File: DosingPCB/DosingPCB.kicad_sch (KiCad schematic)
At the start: 4 parts, among them U1 SHTC3

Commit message: Basically finished schematic
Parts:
- added C1, C4: 22uF, Capacitor_SMD:C_1206_3216Metric, symbol Device:C
- added C2, C5, C6: .1uF, Capacitor_SMD:C_0603_1608Metric, symbol Device:C
- added C3: 10uF, Capacitor_SMD:C_0805_2012Metric, symbol Device:C
- added D1: Green, LED_SMD:LED_0603_1608Metric, symbol Device:LED
- added D2: 1N4148WT, Diode_SMD:D_SOD-523, symbol Diode:1N4148WT
- added D3: 1N5817, Diode_THT:D_DO-41_SOD81_P10.16mm_Horizontal, symbol Diode:1N5817
- added J1: Conn_01x06_Pin, Connector_PinHeader_1.00mm:PinHeader_1x06_P1.00mm_Vertical, symbol Connector:Conn_01x06_Pin
- added J2: STLink, Connector_PinHeader_1.00mm:PinHeader_1x02_P1.00mm_Vertical, symbol Connector:Conn_01x02_Pin
- added J3: Servo Conn, Connector_PinHeader_1.00mm:PinHeader_1x03_P1.00mm_Horizontal, symbol Connector:Conn_01x03_Pin
- added J4: SPI header, Connector_PinHeader_1.00mm:PinHeader_1x08_P1.00mm_Vertical, symbol Connector:Conn_01x08_Pin
- added J5: USB_C_Receptacle_USB2.0_16P, Connector_USB:USB_C_Receptacle_GCT_USB4105-xx-A_16P_TopMnt_Horizontal, symbol Connector:USB_C_Receptacle_USB2.0_16P
- added J8: Solar Cell JST, Connector_JST:JST_PH_S2B-PH-K_1x02_P2.00mm_Horizontal, symbol Connector_Generic:Conn_01x02
- added J9: 5V fan JST, Connector_Molex:Molex_KK-254_AE-6410-03A_1x03_P2.54mm_Vertical, symbol Connector_Generic:Conn_01x03
- added Q1: MMBT2222A, Package_TO_SOT_SMD:SOT-23, symbol Transistor_BJT:MMBT2222A
- added R1: 10k, Resistor_SMD:R_0805_2012Metric, symbol Device:R
- added R2: 470, Resistor_SMD:R_0805_2012Metric, symbol Device:R
- added R3: 1K, Resistor_SMD:R_0805_2012Metric, symbol Device:R
- added R6, R7: 5.1k, Resistor_SMD:R_0805_2012Metric, symbol Device:R
- added SW1: SW_Push, Button_Switch_SMD:SW_SPST_TL3342, symbol Switch:SW_Push
- added SW2: SW_SPDT, Button_Switch_SMD:SW_SPDT_PCM12, symbol Switch:SW_SPDT
- added U1: AMS1117-3.3, Package_TO_SOT_SMD:SOT-223-3_TabPin2, symbol Regulator_Linear:AMS1117-3.3
- added U2: STM32L432KBUx, Package_DFN_QFN:QFN-32-1EP_5x5mm_P0.5mm_EP3.45x3.45mm, symbol MCU_ST_STM32L4:STM32L432KBUx
- added U4: D3V3XA4B10LP, Package_DFN_QFN:Diodes_UDFN-10_1x2.5mm_P0.5mm, symbol Power_Protection:D3V3XA4B10LP
- R4: footprint (none) -> Resistor_SMD:R_0805_2012Metric
- R5: renamed from R3; footprint (none) -> Resistor_SMD:R_0805_2012Metric
- renumbered U1 to U3
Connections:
- net +3.3V: now also C3.1, C4.1, C5.1, C6.1, D1.2 (A), J1.6 (Pin_6), J3.2 (Pin_2), J4.7 (Pin_7), SW2.3 (C), U1.2 (VO), U2.1 (VDD), U2.17 (VDD), U2.5 (VDDA)
- net CS: now also U2.25 (PA15)
- net GND: now also C1.2, C2.1, C3.2, C4.2, C5.2, C6.2, J1.1 (Pin_1), J3.3 (Pin_3), J4.1 (Pin_1), J5.A1 (GND), J5.A12 (GND), J5.B1 (GND), J5.B12 (GND), J5.SH (SHIELD), J8.2 (Pin_2), Q1.2 (E), R2.2, R6.2, R7.2, SW1.1, SW2.1 (A), U1.1 (GND), U2.16 (VSS), U2.32 (VSS), U2.33 (VSS), U4.3 (VSS), U4.8 (VSS)
- net RTC_SCL: now also U2.19 (PA9)
- net RTC_SDA: now also U2.20 (PA10)
- net SD_CLK: now also U2.26 (PB3)
- net SD_DataIn: now also U2.28 (PB5)
- net SD_DataOut: now also U2.27 (PB4)
- net Solar+Charging/VIN/Solar+: now also J8.1 (Pin_1)
- net Temp_SCL: now also U2.29 (PB6)
- net Temp_SDA: now also U2.30 (PB7)
- new net: D2.2 (A), J9.3 (Pin_3), Q1.3 (C)
- new net: Q1.1 (B), R3.2
- new net: J1.2 (Pin_2), U2.2 (PC14)
- new net: J1.3 (Pin_3), U2.3 (PC15)
- new net: J1.4 (Pin_4), U2.14 (PB0)
- new net: J1.5 (Pin_5), U2.15 (PB1)
- new net: R1.2, SW2.2 (B)
- new net: C2.2, SW1.2, U2.4 (NRST)
- new net: J4.2 (Pin_2), U2.13 (PA7)
- new net: J4.3 (Pin_3), U2.12 (PA6)
- new net: J4.4 (Pin_4), U2.11 (PA5)
- new net: J4.5 (Pin_5), U2.10 (PA4)
- new net: J4.6 (Pin_6), U2.7 (PA1)
- new net: J3.1 (Pin_1), U2.18 (PA8)
- new net: J9.1 (Pin_1), U2.9 (PA3)
- new net: R1.1, U2.31 (PH3)
- new net: R3.1, U2.8 (PA2)
- new net: D3.2 (A), J5.A4 (VBUS), J5.A9 (VBUS), J5.B4 (VBUS), J5.B9 (VBUS)
- new net: J5.A5 (CC1), R6.1
- new net: J5.A6 (D+), J5.B6 (D+), U4.1
- new net: J5.A7 (D-), J5.B7 (D-), U4.2, U4.9 (NC)
- new net: J5.B5 (CC2), R7.1
- new net: D1.1 (K), R2.1
- new net +5V: C1.1, D2.1 (K), D3.1 (K), J4.8 (Pin_8), J9.2 (Pin_2), U1.3 (VI)
- new net CD: U2.6 (PA0)
- new net Data+: U2.22 (PA12), U4.5
- new net Data-: U2.21 (PA11), U4.4
- new net SWCLK: J2.1 (Pin_1), U2.24 (PA14)
- new net SWDIO: J2.2 (Pin_2), U2.23 (PA13)
- no-connect marks 0 -> 5
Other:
- sheet SD-Card ports: added CD; removed none
- note added: "Check JST size with Fan and check pin orientation"
- note added: "Check JST size with Solar cell and check pin orientation"
- moved on the sheet: R4, R5, SC1, U3

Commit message: Starting Board setup
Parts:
- D3: footprint Diode_THT:D_DO-41_SOD81_P10.16mm_Horizontal -> Diode_SMD:D_SOD-123
- SW1: footprint Button_Switch_SMD:SW_SPST_TL3342 -> Button_Switch_SMD:SW_Push_SPST_NO_CK_KSC
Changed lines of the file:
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@@
 	)
 	(junction
-		(at 31.75 29.21)
-		(diameter 0)
-		(color 0 0 0 0)
-	)
-	(junction
 		(at 52.07 91.44)
 		(diameter 0)
@@
 	)
 	(junction
-		(at 52.07 26.67)
+		(at 77.47 96.52)
 		(diameter 0)
 		(color 0 0 0 0)
 	)
 	(junction
-		(at 77.47 96.52)
+		(at 254 71.12)
 		(diameter 0)
 		(color 0 0 0 0)
 	)
 	(junction
-		(at 254 71.12)
+		(at 31.75 29.21)
+		(diameter 0)
+		(color 0 0 0 0)
+	)
+	(junction
+		(at 52.07 26.67)
 		(diameter 0)
 		(color 0 0 0 0)
@@
 	(wire
 		(pts
+			(xy 31.75 26.67) (xy 31.75 29.21)
+		)
+		(stroke
+			(width 0)
+			(type default)
+		)
+	)
+	(wire
+		(pts
 			(xy 52.07 99.06) (xy 62.23 99.06)
 		)
@@
 	(wire
 		(pts
-			(xy 52.07 24.13) (xy 52.07 26.67)
+			(xy 52.07 21.59) (xy 52.07 26.67)
 		)
 		(stroke
@@
 		)
 	)
+	(label "5V"
+		(at 31.75 27.94 0)
+		(effects
+			(font
+				(size 1.27 1.27)
+			)
+			(justify left bottom)
+		)
+	)
 	(global_label "Temp_SDA"
 		(shape input)
@@
 		(dnp no)
 		(property "Reference" "SW1"
-			(at 30.48 121.9199 90)
+			(at 14.732 108.458 90)
 			(show_name no)
 			(do_not_autoplace no)
@@
 		)
 		(property "Value" "SW_Push"
-			(at 30.48 124.4599 90)
+			(at 14.732 110.998 90)
 			(show_name no)
 			(do_not_autoplace no)
@@
 			)
 		)
-		(property "Footprint" "Button_Switch_SMD:SW_SPST_TL3342"
+		(property "Footprint" "Button_Switch_SMD:SW_Push_SPST_NO_CK_KSC"
 			(at 21.59 109.22 0)
 			(hide yes)
@@
 	(symbol
 		(lib_id "power:+3.3V")
-		(at 52.07 24.13 0)
+		(at 52.07 21.59 0)
 		(unit 1)
 		(body_style 1)
@@
 		(fields_autoplaced yes)
 		(property "Reference" "#PWR08"
-			(at 52.07 27.94 0)
+			(at 52.07 25.4 0)
 			(hide yes)
 			(show_name no)
@@
 		)
 		(property "Value" "+3.3V"
-			(at 52.07 19.05 0)
+			(at 52.07 16.51 0)
 			(show_name no)
 			(do_not_autoplace no)
@@
 		)
 		(property "Footprint" ""
-			(at 52.07 24.13 0)
+			(at 52.07 21.59 0)
 			(hide yes)
 			(show_name no)
@@
 		)
 		(property "Datasheet" ""
-			(at 52.07 24.13 0)
+			(at 52.07 21.59 0)
 			(hide yes)
 			(show_name no)
@@
 		)
 		(property "Description" "Power symbol creates a global label with name \"+3.3V\""
-			(at 52.07 24.13 0)
+			(at 52.07 21.59 0)
 			(hide yes)
 			(show_name no)
@@
 			)
 		)
-		(property "Footprint" "Diode_THT:D_DO-41_SOD81_P10.16mm_Horizontal"
+		(property "Footprint" "Diode_SMD:D_SOD-123"
 			(at 200.66 89.535 0)
 			(hide yes)
@@
 	(symbol
 		(lib_id "power:+5V")
-		(at 31.75 29.21 0)
+		(at 31.75 26.67 0)
 		(unit 1)
 		(body_style 1)
@@
 		(dnp no)
 		(property "Reference" "#PWR02"
-			(at 31.75 33.02 0)
+			(at 31.75 30.48 0)
 			(hide yes)
 			(show_name no)
@@
 		)
 		(property "Value" "+5V"
-			(at 29.464 24.638 0)
+			(at 29.464 22.098 0)
 			(show_name no)
 			(do_not_autoplace no)
@@
 		)
 		(property "Footprint" ""
-			(at 31.75 29.21 0)
+			(at 31.75 26.67 0)
 			(hide yes)
 			(show_name no)
@@
 		)
 		(property "Datasheet" ""
-			(at 31.75 29.21 0)
+			(at 31.75 26.67 0)
 			(hide yes)
 			(show_name no)
@@
 		)
 		(property "Description" "Power symbol creates a global label with name \"+5V\""
-			(at 31.75 29.21 0)
+			(at 31.75 26.67 0)
 			(hide yes)
 			(show_name no)

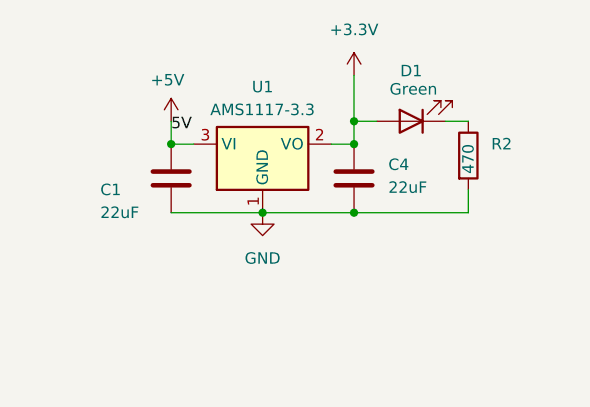
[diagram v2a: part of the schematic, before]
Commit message: Quick RTC fix
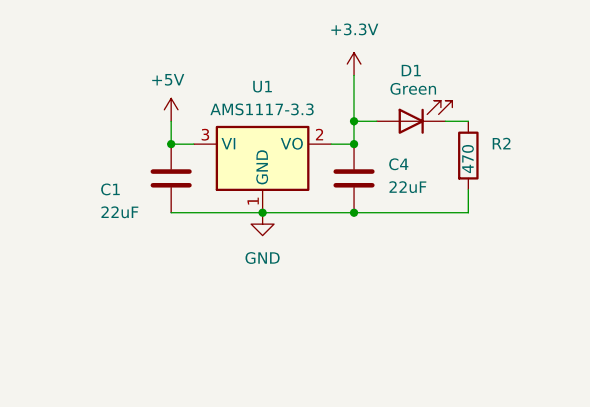
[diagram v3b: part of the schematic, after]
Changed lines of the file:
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@@
-		)
-	)
-	(label "5V"
-		(at 31.75 27.94 0)
-		(effects
-			(font
-				(size 1.27 1.27)
-			)
-			(justify left bottom)
 		)
 	)

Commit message: 98% completed PCB
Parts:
- removed R1: 10k, Resistor_SMD:R_0805_2012Metric, symbol Device:R
- added C16: 10uF, Capacitor_SMD:C_0805_2012Metric, symbol Device:C
- added C17, C25, C26: .1uF, Capacitor_SMD:C_0603_1608Metric, symbol Device:C
- added H4, H5, H6, H7, H8: MountingHole, MountingHole:MountingHole_2.2mm_M2, symbol Mechanical:MountingHole
- added J10, J11: Conn_01x04, Connector_JST:JST_SH_SM04B-SRSS-TB_1x04-1MP_P1.00mm_Horizontal, symbol Connector_Generic:Conn_01x04
- added R26: 10k, Resistor_SMD:R_0805_2012Metric, symbol Device:R
- J1: footprint Connector_PinHeader_1.00mm:PinHeader_1x06_P1.00mm_Vertical -> Connector_PinHeader_2.54mm:PinHeader_1x06_P2.54mm_Vertical
- J2: footprint Connector_PinHeader_1.00mm:PinHeader_1x02_P1.00mm_Vertical -> Connector_PinHeader_2.54mm:PinHeader_1x02_P2.54mm_Vertical
- J3: footprint Connector_PinHeader_1.00mm:PinHeader_1x03_P1.00mm_Horizontal -> Connector_PinHeader_2.54mm:PinHeader_1x03_P2.54mm_Horizontal
- J4: footprint Connector_PinHeader_1.00mm:PinHeader_1x08_P1.00mm_Vertical -> Connector_PinHeader_2.54mm:PinHeader_1x08_P2.54mm_Vertical
- SW1: footprint Button_Switch_SMD:SW_Push_SPST_NO_CK_KSC -> Button_Switch_SMD:SW_Push_SPST_NO_Alps_SKRK
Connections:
- net +3.3V: now also C16.2, C17.1, C25.1, J10.2 (Pin_2), J11.3 (Pin_3); no longer J3.2 (Pin_2)
- net +5V: now also J3.2 (Pin_2), C26.1
- net CD: now also U2.14 (PB0); no longer U2.6 (PA0)
- net GND: now also C16.1, C17.2, C25.2, C26.2, J10.1 (Pin_1), J11.4 (Pin_4), R26.1
- net Temp_SCL: now also R4.1, U3.3 (SDA), J10.4 (Pin_4), J11.1 (Pin_1); no longer R5.1, U3.2 (SCL)
- net Temp_SDA: now also R5.1, U3.2 (SCL), J10.3 (Pin_3), J11.2 (Pin_2); no longer R4.1, U3.3 (SDA)
- net header conn: now reaches J1.4 (Pin_4)
- net header conn: now also U2.6 (PA0); no longer U2.14 (PB0)
- net at SW2.2 (B): now also U2.31 (PH3), R26.2
- net Solar+Charging/VIN/Solar+ renamed Solar_power
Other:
- moved on the sheet: C1, C4, D1, D3, J8, R2, U1

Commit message: Finished PCB - mousebites
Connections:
- net at J1.5 (Pin_5): no longer U2.15 (PB1)
- net header conn: no longer names the net of J1.4 (Pin_4)
- net header conn: no longer U2.6 (PA0)
- no-connect marks 5 -> 9
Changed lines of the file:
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@@
+	)
+	(no_connect
+		(at 92.71 104.14)
 	)
 	(no_connect
@@
 	)
 	(no_connect
+		(at 66.04 168.91)
+	)
+	(no_connect
 		(at 208.28 133.35)
+	)
+	(no_connect
+		(at 67.31 124.46)
 	)
 	(no_connect
@@
 		(at 198.12 125.73)
 	)
+	(no_connect
+		(at 63.5 168.91)
+	)
 	(wire
 		(pts
@@
 	(wire
 		(pts
-			(xy 66.04 124.46) (xy 66.04 168.91)
-		)
-		(stroke
-			(width 0)
-			(type default)
-		)
-	)
-	(wire
-		(pts
 			(xy 219.71 27.94) (xy 223.52 27.94)
 		)
@@
 		(pts
 			(xy 31.75 137.16) (xy 31.75 142.24)
-		)
-		(stroke
-			(width 0)
-			(type default)
-		)
-	)
-	(wire
-		(pts
-			(xy 67.31 124.46) (xy 66.04 124.46)
 		)
 		(stroke
@@
 		)
 	)
-	(global_label "header conn"
-		(shape input)
-		(at 63.5 168.91 90)
-		(fields_autoplaced yes)
-		(effects
-			(font
-				(size 1.27 1.27)
-			)
-			(justify left)
-		)
-		(property "Intersheetrefs" "${INTERSHEET_REFS}"
-			(at 63.5 154.0112 90)
-			(hide yes)
-			(show_name no)
-			(do_not_autoplace no)
-			(effects
-				(font
-					(size 1.27 1.27)
-				)
-				(justify left)
-			)
-		)
-	)
 	(global_label "CS"
 		(shape input)
@@
 			(hide yes)
 			(show_name no)
-			(do_not_autoplace no)
-			(effects
-				(font
-					(size 1.27 1.27)
-				)
-				(justify left)
-			)
-		)
-	)
-	(global_label "header conn"
-		(shape input)
-		(at 92.71 104.14 0)
-		(fields_autoplaced yes)
-		(effects
-			(font
-				(size 1.27 1.27)
-			)
-			(justify left)
-		)
-		(property "Intersheetrefs" "${INTERSHEET_REFS}"
-			(at 107.6088 104.14 0)
-			(hide yes)
-			(show_name no)
